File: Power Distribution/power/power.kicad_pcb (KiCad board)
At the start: 2 copper layers, 148.3 x 25.4 mm, 20 parts, among them J1 Conn_01x01_Socket, J10 Conn_02x05_Odd_Even, J11 Conn_02x05_Odd_Even, J12 Conn_02x05_Odd_Even, J13 Conn_02x05_Odd_Even, J14 Conn_02x05_Odd_Even, J15 Conn_02x05_Odd_Even, J16 Conn_02x05_Odd_Even, J2 Conn_01x01_Socket, J3 Conn_01x01_Socket, J4 Conn_01x01_Socket, J5 Conn_01x01_Socket, J6 Conn_01x01_Socket, J7 Conn_02x05_Odd_Even, J8 Conn_02x05_Odd_Even, J9 Conn_02x05_Odd_Even

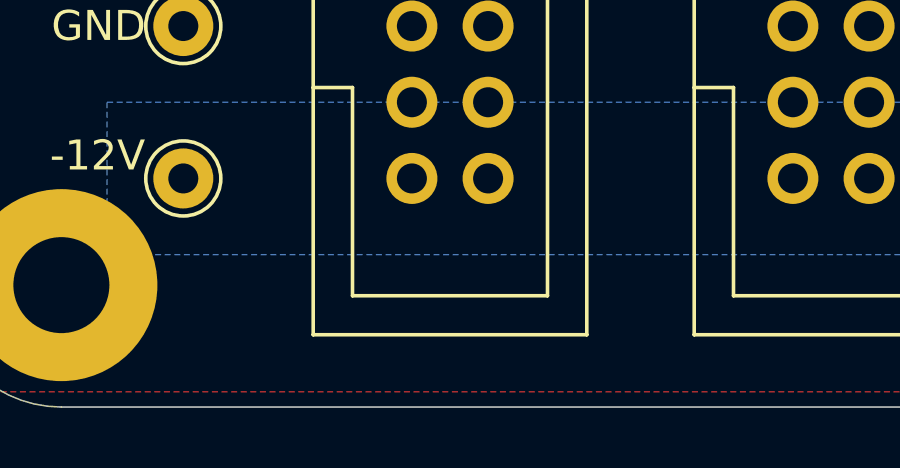
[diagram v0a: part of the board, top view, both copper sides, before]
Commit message: JLCPCB order number template
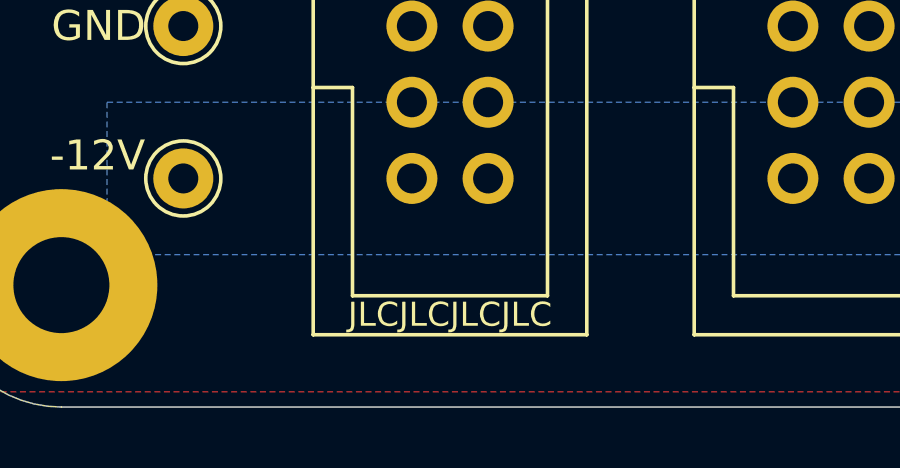
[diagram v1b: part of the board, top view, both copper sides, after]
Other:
- board text added: "JLCJLCJLCJLC"
